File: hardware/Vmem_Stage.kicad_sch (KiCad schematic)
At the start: 0 parts

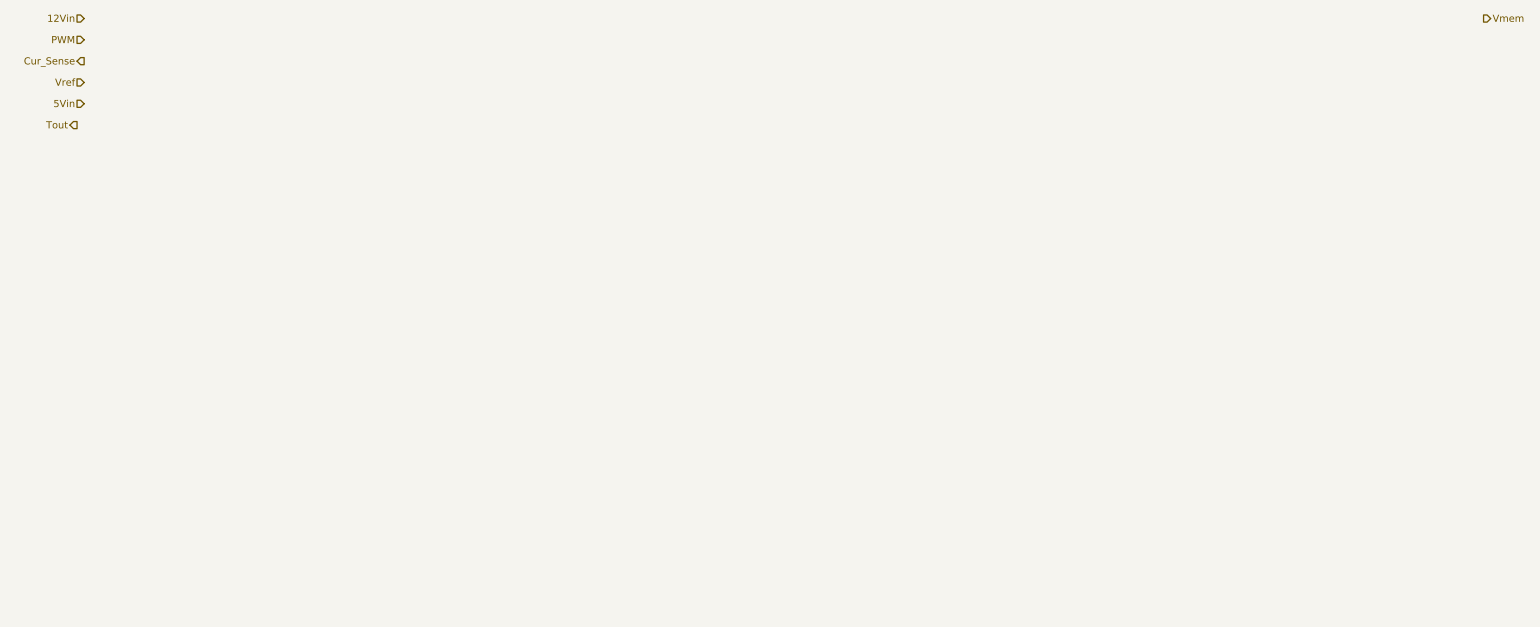
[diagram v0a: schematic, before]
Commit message: feat(schematic): Vmem schematic completed, connected controler and stages on main
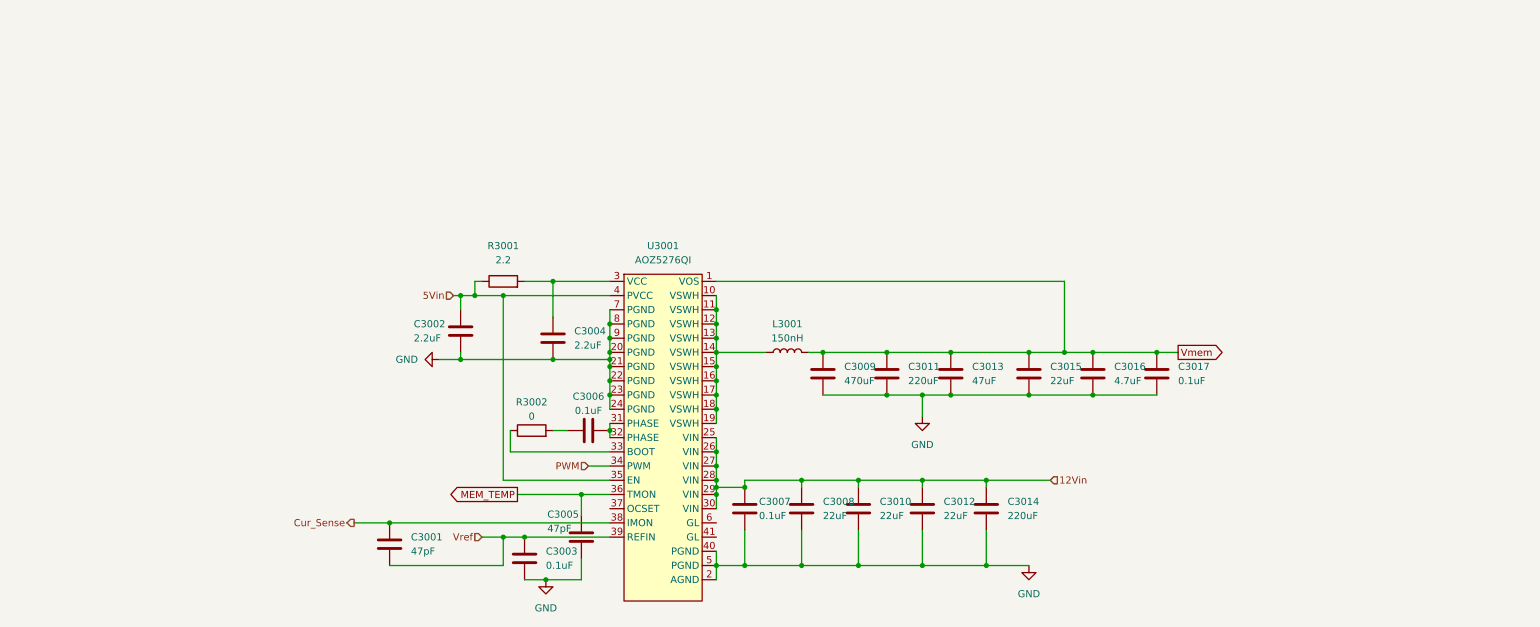
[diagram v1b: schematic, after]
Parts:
- added C3001, C3005: 47pF, Capacitor_SMD:C_0805_2012Metric, symbol Device:C
- added C3002, C3004: 2.2uF, Capacitor_SMD:C_0805_2012Metric, symbol Device:C
- added C3003, C3006, C3007, C3017: 0.1uF, Capacitor_SMD:C_0805_2012Metric, symbol Device:C
- added C3008, C3010, C3012, C3015: 22uF, Capacitor_SMD:C_0805_2012Metric, symbol Device:C
- added C3009: 470uF, work:CP_EIA-7343-40_Kemet-Y, symbol Device:C
- added C3011, C3014: 220uF, Capacitor_THT:CP_Radial_D6.3mm_P2.50mm, symbol Device:C
- added C3013: 47uF, Capacitor_SMD:C_0805_2012Metric, symbol Device:C
- added C3016: 4.7uF, Capacitor_SMD:C_0805_2012Metric, symbol Device:C
- added L3001: 150nH, work:IND_IHVR-4025JZ-3Z_VIS, symbol Device:L
- added R3001: 2.2, Resistor_SMD:R_0805_2012Metric, symbol Device:R
- added R3002: 0, Resistor_SMD:R_0805_2012Metric, symbol Device:R
- added U3001: AOZ5276QI, work:AOZ5276QI, symbol Symbol_Library:AOZ5276QI
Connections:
- net 12Vin: now also C3007.1, C3008.1, C3010.1, C3012.1, C3014.1, U3001.25 (VIN), U3001.26 (VIN), U3001.27 (VIN), U3001.28 (VIN), U3001.29 (VIN), U3001.30 (VIN)
- net 5Vin: now also C3002.1, R3001.1, U3001.35 (EN), U3001.4 (PVCC)
- net Cur_Sense: now also C3001.1, U3001.38 (IMON)
- net PWM: now also U3001.34 (PWM)
- net Vmem: now also C3009.1, C3011.1, C3013.1, C3015.1, C3016.1, C3017.1, L3001.2, U3001.1 (VOS)
- net Vref: now also C3001.2, C3003.1, U3001.39 (REFIN)
- new net: C3004.1, R3001.2, U3001.3 (VCC)
- new net: R3002.1, U3001.33 (BOOT)
- new net: C3006.1, R3002.2
- new net: L3001.1, U3001.10 (VSWH), U3001.11 (VSWH), U3001.12 (VSWH), U3001.13 (VSWH), U3001.14 (VSWH), U3001.15 (VSWH), U3001.16 (VSWH), U3001.17 (VSWH), U3001.18 (VSWH), U3001.19 (VSWH)
- new net: C3006.2, U3001.31 (PHASE), U3001.32 (PHASE)
- new net GND: C3002.2, C3003.2, C3004.2, C3005.2, C3007.2, C3008.2, C3009.2, C3010.2, C3011.2, C3012.2, C3013.2, C3014.2, C3015.2, C3016.2, C3017.2, U3001.2 (AGND), U3001.20 (PGND), U3001.21 (PGND), U3001.22 (PGND), U3001.23 (PGND), U3001.24 (PGND), U3001.40 (PGND), U3001.5 (PGND), U3001.7 (PGND), U3001.8 (PGND), U3001.9 (PGND)
- new net MEM_TEMP: C3005.1, U3001.36 (TMON)

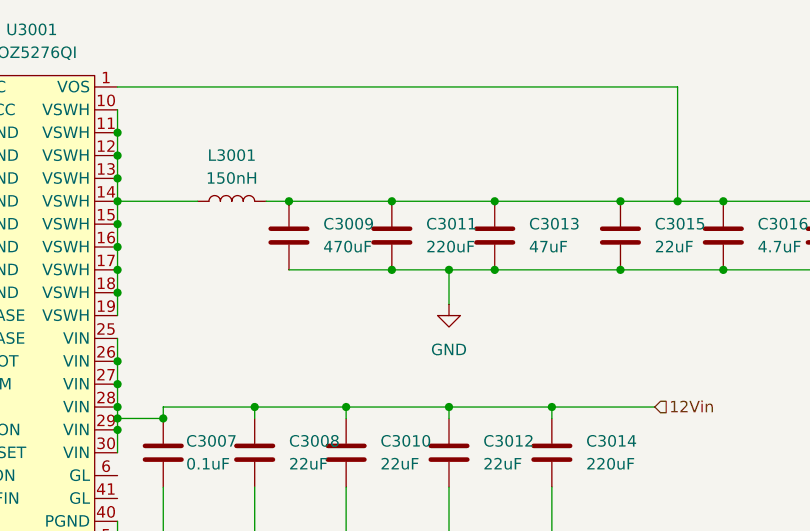
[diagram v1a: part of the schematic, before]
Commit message: feat(PCB): Vrms for mem and core layed out
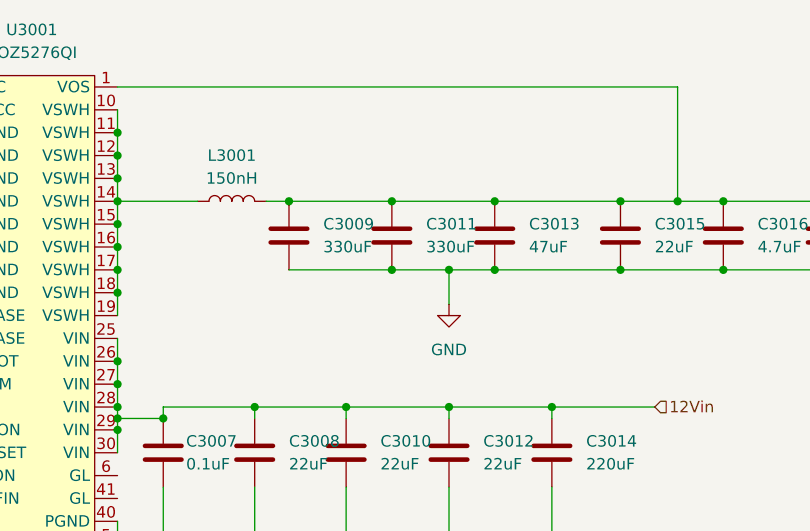
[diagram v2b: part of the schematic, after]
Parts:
- C3009: value 470uF -> 330uF
- C3011: value 220uF -> 330uF; footprint Capacitor_THT:CP_Radial_D6.3mm_P2.50mm -> work:CP_EIA-7343-40_Kemet-Y
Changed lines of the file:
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@@
 			)
 		)
-		(property "Value" "470uF"
+		(property "Value" "330uF"
 			(at 161.29 83.8199 0)
 			(effects
@@
 			)
 		)
-		(property "Datasheet" "https://www.digikey.com/en/products/detail/panasonic-electronic-components/EEF-SX0D471XE/1731681"
+		(property "Datasheet" ""
 			(at 157.48 82.55 0)
 			(effects
@@
 			)
 		)
-		(property "Value" "220uF"
+		(property "Value" "330uF"
 			(at 172.72 83.8199 0)
 			(effects
@@
 			)
 		)
-		(property "Footprint" "Capacitor_THT:CP_Radial_D6.3mm_P2.50mm"
+		(property "Footprint" "work:CP_EIA-7343-40_Kemet-Y"
 			(at 169.8752 86.36 0)
 			(effects
@@
 			)
 		)
-		(property "Datasheet" "https://www.digikey.com/en/products/detail/kyocera-avx/RPA0608221M016B/17634426"
+		(property "Datasheet" ""
 			(at 168.91 82.55 0)
 			(effects

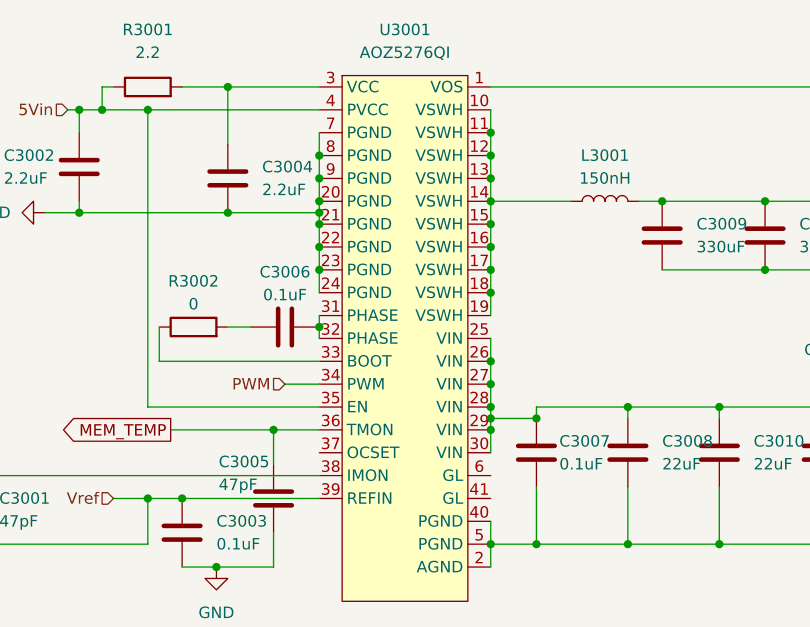
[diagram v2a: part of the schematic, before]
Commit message: feat(PCB): fix all DRC errors
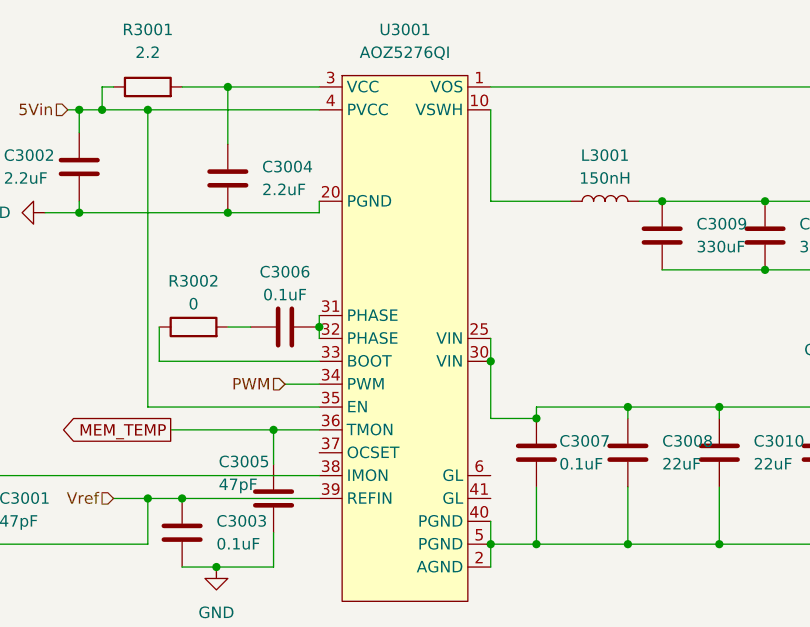
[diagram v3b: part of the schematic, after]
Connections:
- net 12Vin: no longer U3001.26 (VIN), U3001.27 (VIN), U3001.28 (VIN), U3001.29 (VIN)
- net GND: no longer U3001.21 (PGND), U3001.22 (PGND), U3001.23 (PGND), U3001.24 (PGND), U3001.7 (PGND), U3001.8 (PGND), U3001.9 (PGND)
- new net: L3001.1, U3001.10 (VSWH)

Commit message: feat(schematic): added cooler mounting holes
added cooler mounting holes to schematic
changed temp pins to read proper tempurature
small fixes
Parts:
- removed C3005: 47pF, Capacitor_SMD:C_0805_2012Metric, symbol Device:C
- C3001, C3002, C3003, C3004, C3006, C3007, C3015, C3016, C3017: footprint Capacitor_SMD:C_0805_2012Metric -> Capacitor_SMD:C_0402_1005Metric
- C3010: value 22uF -> 47uF; footprint Capacitor_SMD:C_0805_2012Metric -> Capacitor_SMD:C_1210_3225Metric
- C3014: footprint Capacitor_THT:CP_Radial_D6.3mm_P2.50mm -> Capacitor_SMD:CP_Elec_6.3x7.7
- R3001, R3002: footprint Resistor_SMD:R_0805_2012Metric -> Resistor_SMD:R_0402_1005Metric
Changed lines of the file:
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@@
-	)
-	(junction
-		(at 107.95 119.38)
-		(diameter 0)
-		(color 0 0 0 0)
 	)
 	(junction
@@
 		(color 0 0 0 0)
 	)
-	(junction
-		(at 114.3 104.14)
-		(diameter 0)
-		(color 0 0 0 0)
-	)
 	(wire
 		(pts
@@
 	(wire
 		(pts
-			(xy 114.3 104.14) (xy 119.38 104.14)
+			(xy 102.87 104.14) (xy 119.38 104.14)
 		)
 		(stroke
@@
 	(wire
 		(pts
-			(xy 102.87 104.14) (xy 114.3 104.14)
-		)
-		(stroke
-			(width 0)
-			(type default)
-		)
-	)
-	(wire
-		(pts
 			(xy 92.71 68.58) (xy 95.25 68.58)
 		)
@@
 	(wire
 		(pts
-			(xy 114.3 107.95) (xy 114.3 104.14)
-		)
-		(stroke
-			(width 0)
-			(type default)
-		)
-	)
-	(wire
-		(pts
 			(xy 186.69 116.84) (xy 175.26 116.84)
 		)
@@
 	(wire
 		(pts
-			(xy 114.3 119.38) (xy 107.95 119.38)
-		)
-		(stroke
-			(width 0)
-			(type default)
-		)
-	)
-	(wire
-		(pts
 			(xy 109.22 66.04) (xy 119.38 66.04)
 		)
@@
 		(pts
 			(xy 153.67 110.49) (xy 153.67 116.84)
-		)
-		(stroke
-			(width 0)
-			(type default)
-		)
-	)
-	(wire
-		(pts
-			(xy 114.3 115.57) (xy 114.3 119.38)
 		)
 		(stroke
@@
 			)
 		)
-		(property "Footprint" "Capacitor_SMD:C_0805_2012Metric"
+		(property "Footprint" "Capacitor_SMD:C_0402_1005Metric"
 			(at 93.6752 78.74 0)
 			(effects
@@
 			)
 		)
-		(property "Datasheet" "~"
+		(property "Datasheet" "https://jlcpcb.com/partdetail/13164-CL05A225MQ5NSNC/C12530"
 			(at 92.71 74.93 0)
 			(effects
@@
 			)
 		)
-		(property "Datasheet" ""
+		(property "Datasheet" "https://jlcpcb.com/partdetail/Panasonic-EEFCX0E331R/C165969"
 			(at 157.48 82.55 0)
 			(effects
@@
 			)
 		)
-		(property "Footprint" "Capacitor_THT:CP_Radial_D6.3mm_P2.50mm"
+		(property "Footprint" "Capacitor_SMD:CP_Elec_6.3x7.7"
 			(at 187.6552 110.49 0)
 			(effects
@@
 			)
 		)
-		(property "Datasheet" "https://www.digikey.com/en/products/detail/kyocera-avx/RPA0608221M016B/17634426"
+		(property "Datasheet" "https://jlcpcb.com/partdetail/HonorElec-RVT1C221M0607/C3342"
 			(at 186.69 106.68 0)
 			(effects
@@
 			)
 		)
-		(property "Footprint" "Capacitor_SMD:C_0805_2012Metric"
+		(property "Footprint" "Capacitor_SMD:C_0402_1005Metric"
 			(at 218.1352 86.36 0)
 			(effects
@@
 			)
 		)
-		(property "Datasheet" "~"
+		(property "Datasheet" "https://jlcpcb.com/partdetail/1933-0402F104M500NT/C1581"
 			(at 217.17 82.55 0)
 			(effects
@@
 			)
 		)
-		(property "Footprint" "Capacitor_SMD:C_0805_2012Metric"
+		(property "Footprint" "Capacitor_SMD:C_0402_1005Metric"
 			(at 195.2752 86.36 0)
 			(effects
@@
 			)
 		)
-		(property "Datasheet" "~"
+		(property "Datasheet" "https://jlcpcb.com/partdetail/Chinocera-HGC0402R5226M6R3NTEJ/C7432764"
 			(at 194.31 82.55 0)
 			(effects
@@
 			)
 		)
-		(property "Footprint" "Resistor_SMD:R_0805_2012Metric"
+		(property "Footprint" "Resistor_SMD:R_0402_1005Metric"
 			(at 100.33 67.818 90)
 			(effects
@@
 			)
 		)
-		(property "Datasheet" "~"
+		(property "Datasheet" "https://jlcpcb.com/partdetail/25901-0402WGJ022JTCE/C25158"
 			(at 100.33 66.04 0)
 			(effects
@@
 			)
 		)
-		(property "Footprint" "Resistor_SMD:R_0805_2012Metric"
+		(property "Footprint" "Resistor_SMD:R_0402_1005Metric"
 			(at 105.41 94.488 90)
 			(effects
@@
 			)
 		)
-		(property "Datasheet" "~"
+		(property "Datasheet" "https://jlcpcb.com/partdetail/17853-0402WGF0000TCE/C17168"
 			(at 105.41 92.71 0)
 			(effects
@@
 			)
 		)
-		(property "Value" "22uF"
+		(property "Value" "47uF"
 			(at 167.64 107.9499 0)
 			(effects
@@
 			)
 		)
-		(property "Footprint" "Capacitor_SMD:C_0805_2012Metric"
+		(property "Footprint" "Capacitor_SMD:C_1210_3225Metric"
 			(at 164.7952 110.49 0)
 			(effects
@@
 			)
 		)
-		(property "Datasheet" "~"
+		(property "Datasheet" "https://jlcpcb.com/partdetail/MurataElectronics-GRM32ER61C476KE15L/C77101"
 			(at 163.83 106.68 0)
 			(effects
@@
 			)
 		)
-		(property "Footprint" "Capacitor_SMD:C_0805_2012Metric"
+		(property "Footprint" "Capacitor_SMD:C_0402_1005Metric"
 			(at 110.1852 80.01 0)
 			(effects
@@
 			)
 		)
-		(property "Datasheet" "~"
+		(property "Datasheet" "https://jlcpcb.com/partdetail/13164-CL05A225MQ5NSNC/C12530"
 			(at 109.22 76.2 0)
 			(effects
@@
 			)
 		)
-		(property "Datasheet" "~"
+		(property "Datasheet" "https://jlcpcb.com/partdetail/17464-CL21A476MQYNNNE/C16780"
 			(at 180.34 82.55 0)
 			(effects
@@
 				(path "/d5303413-7068-41ba-88e3-39dfa38d31b7/9f68ccd3-0983-4a5e-b653-3439cd2061d4"
 					(reference "C9013")
-					(unit 1)
-				)
-			)
-		)
-	)
-	(symbol
-		(lib_id "Device:C")
-		(at 114.3 111.76 0)
-		(unit 1)
-		(exclude_from_sim no)
-		(in_bom yes)
-		(on_board yes)
-		(dnp no)
-		(property "Reference" "C3005"
-			(at 108.204 107.696 0)
-			(effects
-				(font
-					(size 1.27 1.27)
-				)
-				(justify left)
-			)
-		)
-		(property "Value" "47pF"
-			(at 108.204 110.236 0)
-			(effects
-				(font
-					(size 1.27 1.27)
-				)
-				(justify left)
-			)
-		)
-		(property "Footprint" "Capacitor_SMD:C_0805_2012Metric"
-			(at 115.2652 115.57 0)
-			(effects
-				(font
-					(size 1.27 1.27)
-				)
-				(hide yes)
-			)
-		)
-		(property "Datasheet" "~"
-			(at 114.3 111.76 0)
-			(effects
-				(font
-					(size 1.27 1.27)
-				)
-				(hide yes)
-			)
-		)
-		(property "Description" "Unpolarized capacitor"
-			(at 114.3 111.76 0)
-			(effects
-				(font
-					(size 1.27 1.27)
-				)
-				(hide yes)
-			)
-		)
-		(pin "2"
-		)
-		(pin "1"
-		)
-		(instances
-			(project "gpu-external-power-supply"
-				(path "/d5303413-7068-41ba-88e3-39dfa38d31b7/7e7f036f-1da2-41a9-8561-b6e0c1145c03"
-					(reference "C3005")
-					(unit 1)
-				)
-				(path "/d5303413-7068-41ba-88e3-39dfa38d31b7/9f68ccd3-0983-4a5e-b653-3439cd2061d4"
-					(reference "C9005")
 					(unit 1)
 				)
@@
 			)
 		)
-		(property "Datasheet" "~"
+		(property "Datasheet" "https://jlcpcb.com/partdetail/46786-CL21A226MAQNNNE/C45783"
 			(at 153.67 106.68 0)
 			(effects
@@
 			)
 		)
-		(property "Footprint" "Capacitor_SMD:C_0805_2012Metric"
+		(property "Footprint" "Capacitor_SMD:C_0402_1005Metric"
 			(at 144.4752 110.49 0)
 			(effects
@@
 			)
 		)
-		(property "Datasheet" "~"
+		(property "Datasheet" "https://jlcpcb.com/partdetail/1933-0402F104M500NT/C1581"
 			(at 143.51 106.68 0)
 			(effects
@@
 			)
 		)
-		(property "Datasheet" "~"
+		(property "Datasheet" "https://jlcpcb.com/partdetail/46786-CL21A226MAQNNNE/C45783"
 			(at 175.26 106.68 0)
 			(effects
@@
 			)
 		)
-		(property "Footprint" "Capacitor_SMD:C_0805_2012Metric"
+		(property "Footprint" "Capacitor_SMD:C_0402_1005Metric"
 			(at 80.9752 116.84 0)
 			(effects
@@
 			)
 		)
-		(property "Datasheet" "~"
+		(property "Datasheet" "https://jlcpcb.com/partdetail/1919-0402CG470J500NT/C1567"
 			(at 80.01 113.03 0)
 			(effects
@@
 			)
 		)
-		(property "Footprint" "Capacitor_SMD:C_0805_2012Metric"
+		(property "Footprint" "Capacitor_SMD:C_0402_1005Metric"
 			(at 206.7052 86.36 0)
 			(effects
@@
 			)
 		)
-		(property "Datasheet" "~"
+		(property "Datasheet" "https://jlcpcb.com/partdetail/24469-CL05A475MP5NRNC/C23733"
 			(at 205.74 82.55 0)
 			(effects
@@
 			)
 		)
-		(property "Footprint" "Capacitor_SMD:C_0805_2012Metric"
+		(property "Footprint" "Capacitor_SMD:C_0402_1005Metric"
 			(at 105.1052 119.38 0)
 			(effects
@@
 			)
 		)
-		(property "Datasheet" "~"
+		(property "Datasheet" "https://jlcpcb.com/partdetail/1933-0402F104M500NT/C1581"
 			(at 104.14 115.57 0)
 			(effects
@@
 			)
 		)
-		(property "Footprint" "Capacitor_SMD:C_0805_2012Metric"
+		(property "Footprint" "Capacitor_SMD:C_0402_1005Metric"
 			(at 119.38 91.7448 0)
 			(effects
@@
 			)
 		)
-		(property "Datasheet" "~"
+		(property "Datasheet" "https://jlcpcb.com/partdetail/1933-0402F104M500NT/C1581"
 			(at 115.57 92.71 0)
 			(effects
@@
 			)
 		)
-		(property "Datasheet" ""
+		(property "Datasheet" "https://jlcpcb.com/partdetail/Panasonic-EEFCX0E331R/C165969"
 			(at 168.91 82.55 0)
 			(effects
